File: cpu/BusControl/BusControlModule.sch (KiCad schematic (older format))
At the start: 1 part

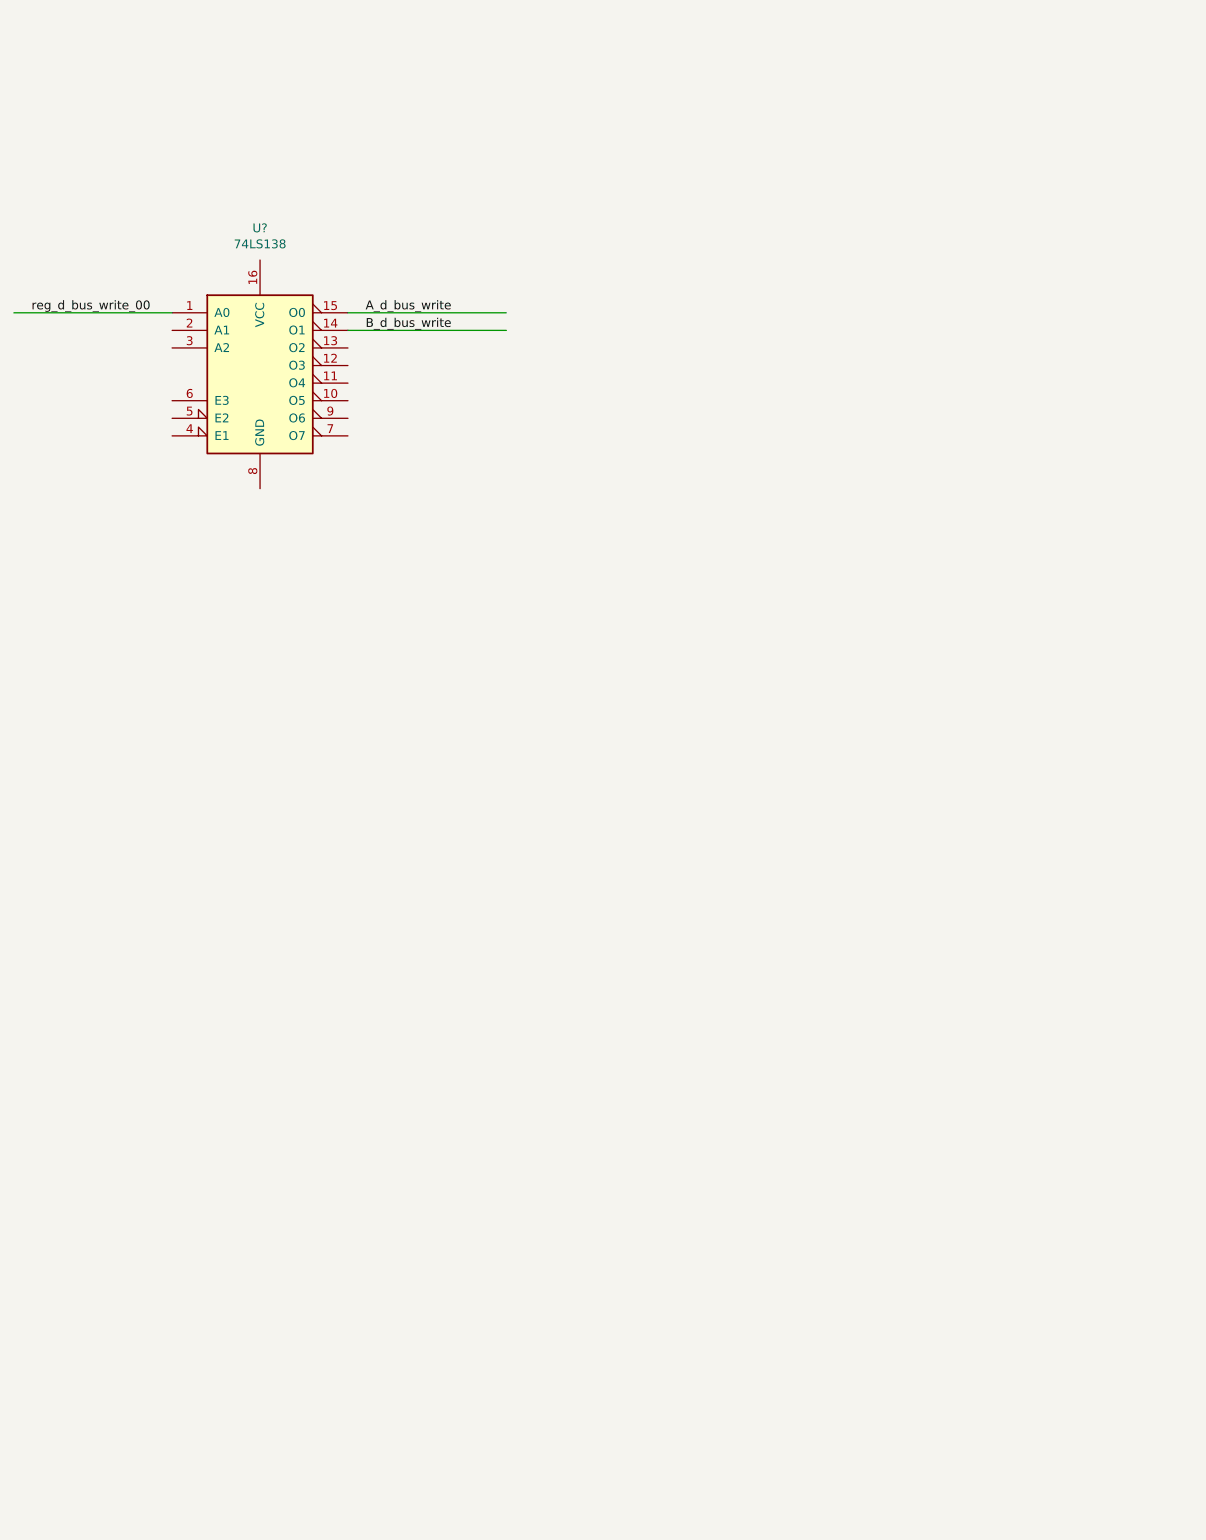
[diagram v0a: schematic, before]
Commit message: Part 1 of Bus Control (DBUS read/write)
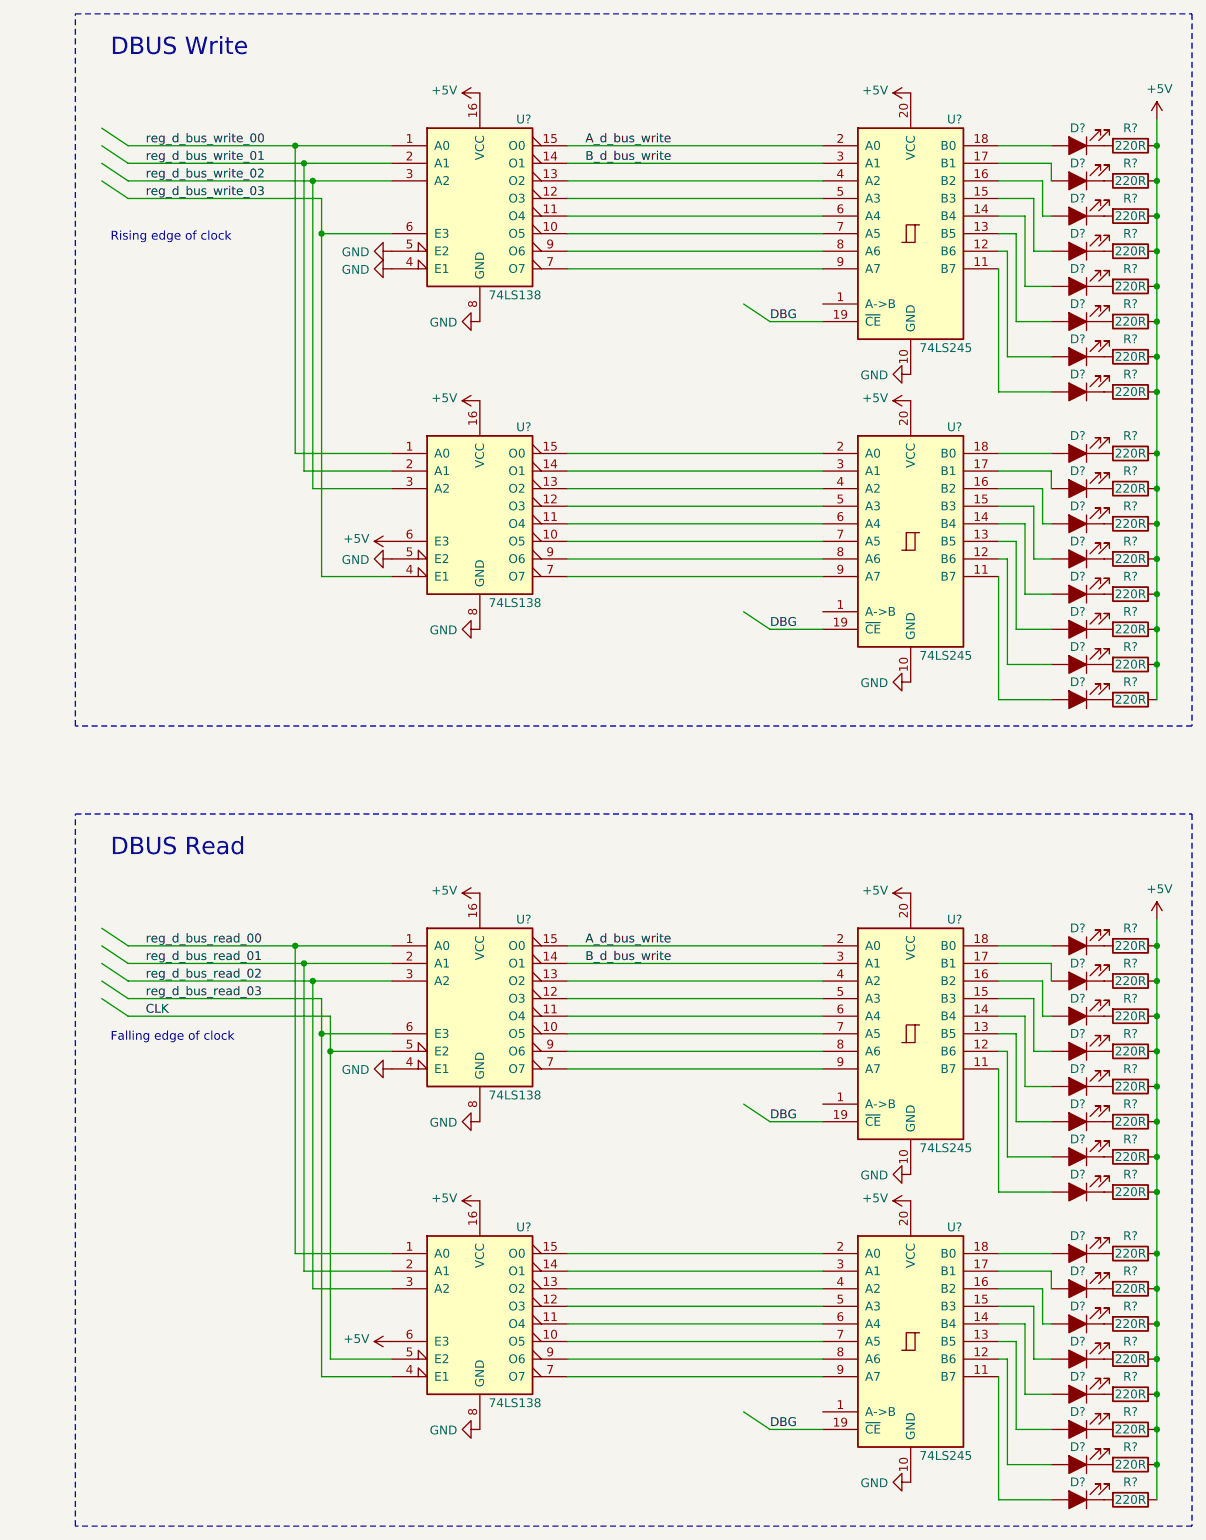
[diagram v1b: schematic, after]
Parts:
- added D? (x32): LED_ALT, symbol Device:LED_ALT
- added R? (x32): 220R, symbol Device:R
- added U? (x3): 74LS138, symbol 74xx:74LS138
- added U? (x4): 74LS245, symbol 74ls245_bidirection:74LS245_BiDirection
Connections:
- net labels added: +5V, CLK, DBG, GND, reg_d_bus_read_00, reg_d_bus_read_01, reg_d_bus_read_02, reg_d_bus_read_03, reg_d_bus_write_01, reg_d_bus_write_02, reg_d_bus_write_03
- wire segments 3 -> 200
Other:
- note added: "DBUS Read"
- note added: "DBUS Write"
- note added: "Falling edge of clock"
- note added: "Rising edge of clock"
- moved on the sheet: U?
